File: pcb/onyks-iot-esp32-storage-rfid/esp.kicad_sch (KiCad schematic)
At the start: 16 parts, among them J2 Conn_01x06_Pin, J3 Conn_02x05_Top_Bottom, Q1 SS8050, Q2 SS8050, SW3 SW_Push, SW4 SW_Push, U1 ESP32-WROOM-32D

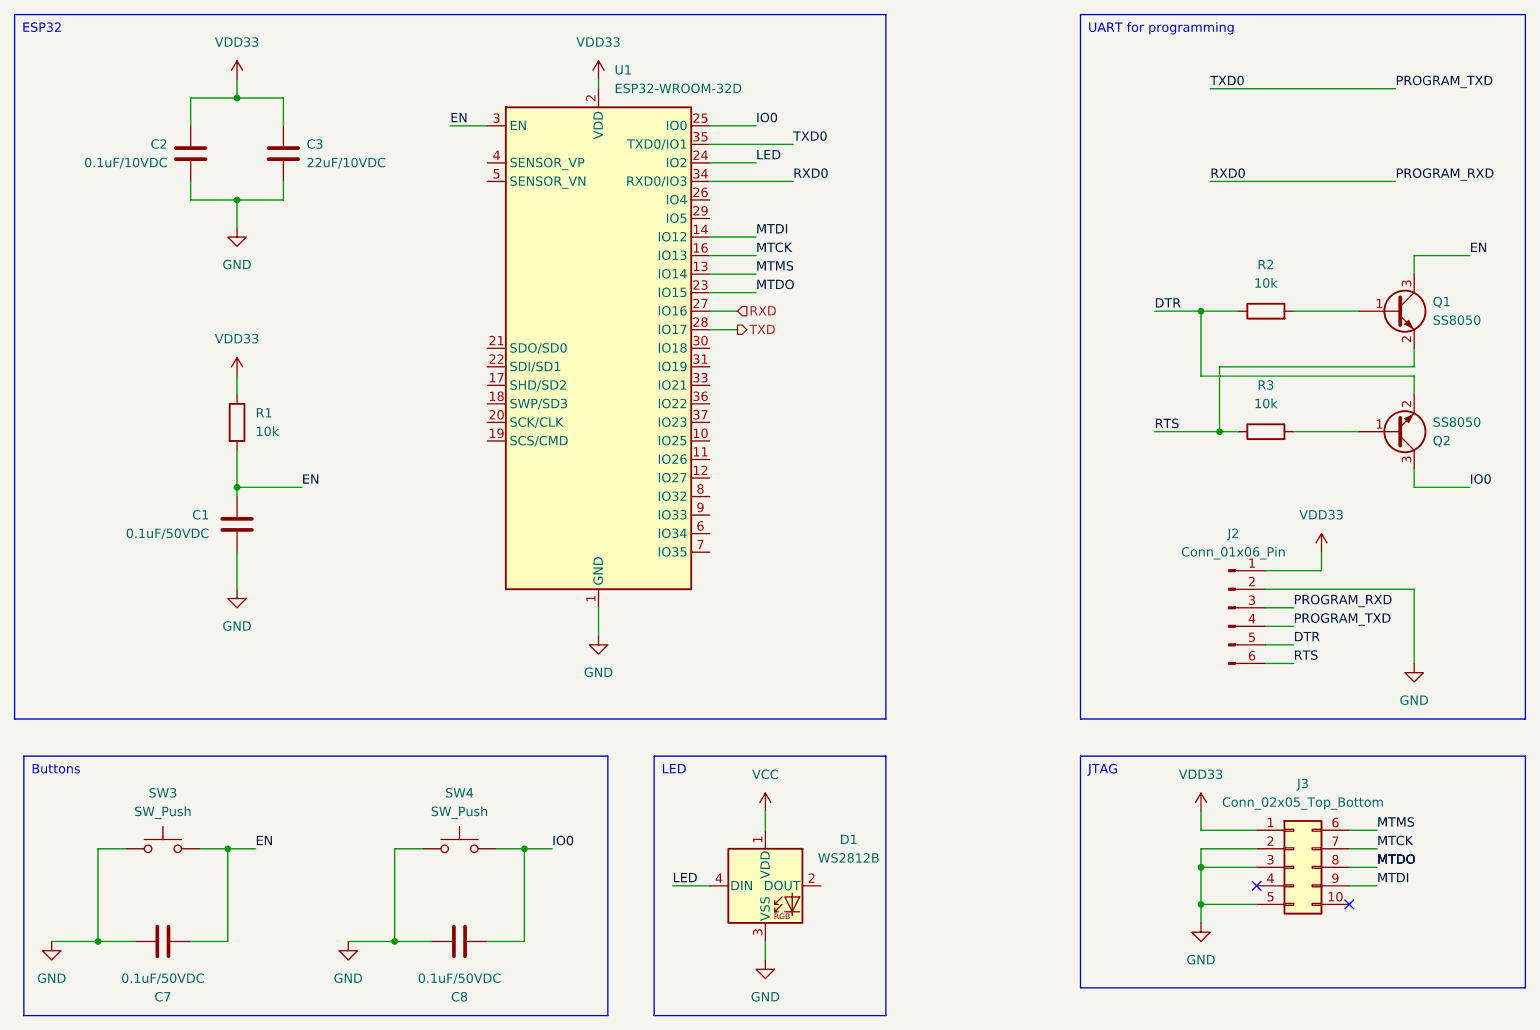
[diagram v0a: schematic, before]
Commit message: oznaczenie pinów i podział elementów PCB
dodanie oznaczenia nieużywanych pinów zgodnie z opinią schematu
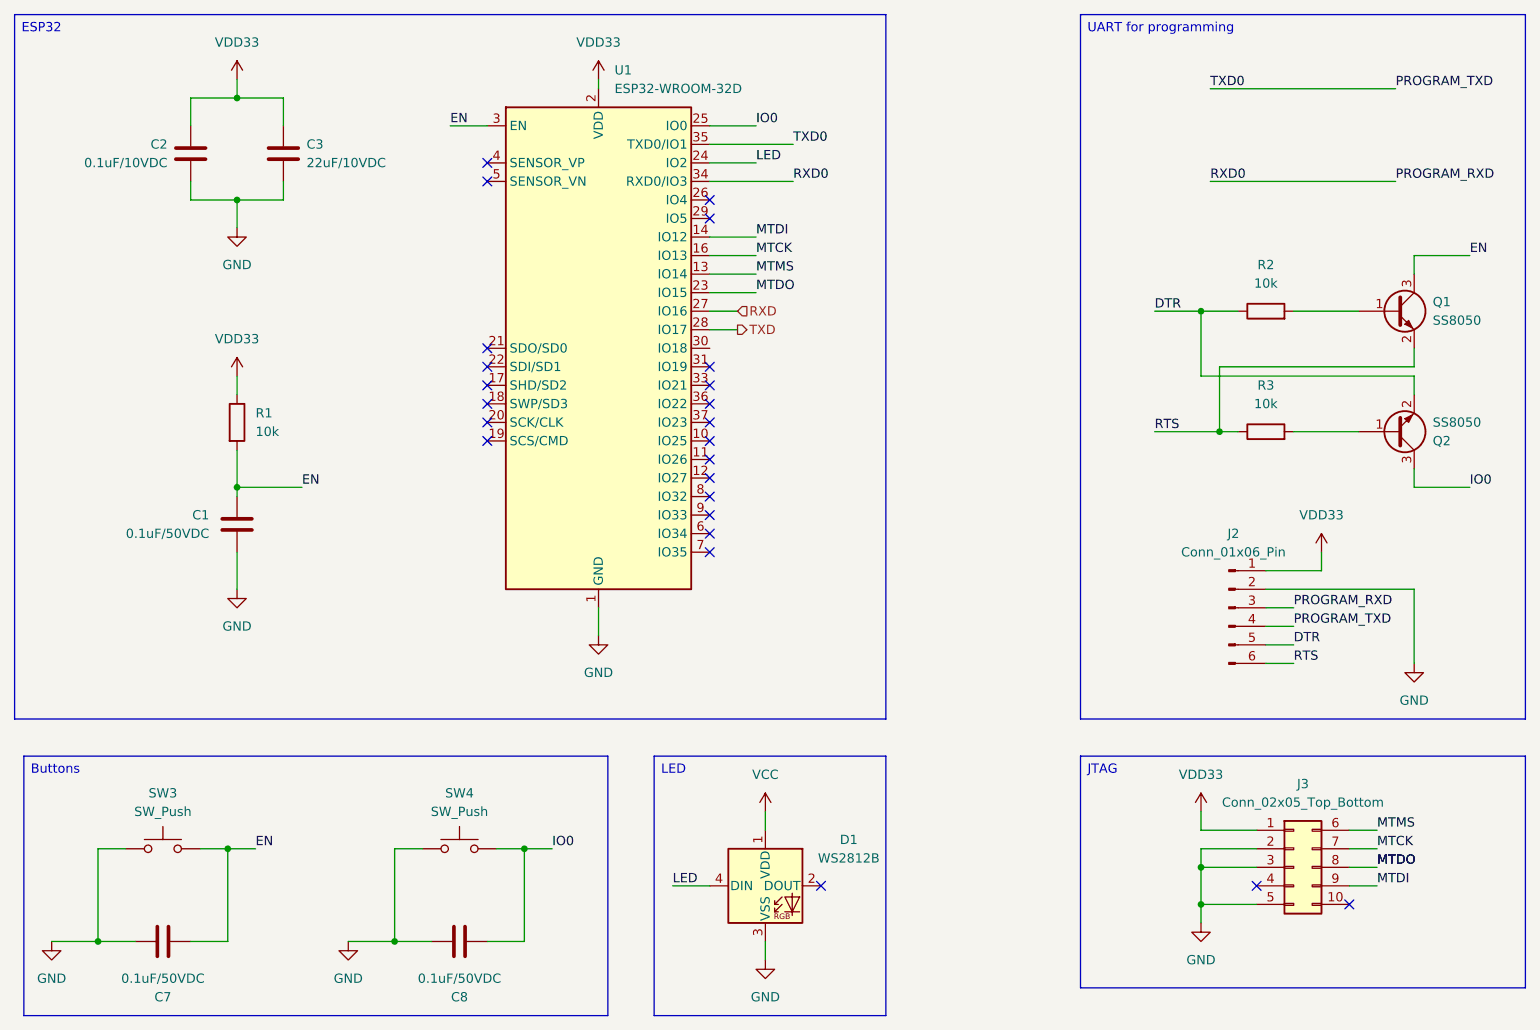
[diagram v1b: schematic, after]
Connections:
- no-connect marks 2 -> 24

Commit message: zrobione review, wprowadzone poprawki, czeka na ostatnie sprawdzenie jak prezes bedzie bardizej przytomny
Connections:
- no-connect marks 24 -> 25
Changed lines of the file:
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@@
+	)
+	(no_connect
+		(at 135.89 64.77)
 	)
 	(no_connect
